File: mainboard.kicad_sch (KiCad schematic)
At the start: 94 parts, among them J1 Conn 02x05 1.27mm, J2 TMS-110-01-G-S, J3 SFMC-110-01-L-D, J4 CLP-105-02-X-DH-A, J5 CLP-105-02-X-DH-A, J6 CLP-105-02-X-DH-A, J7 CLP-105-02-X-DH-A, J8 U.FL-R-SMT-1, J9 USB_C_Receptacle_USB2.0, SW1 KMR231NG, SW2 SW_SPDT, U1 ATSAMD51J20A-M, U10 USBLC6-2SC6, U11 PCF8523TK, U2 MAX706RESA+, U3 AP2112K-3.3, U4 MR25H40, U5 BMX160, U6 RFM98PW, U7 DRV8830DRC, U8 DRV8830DRC, U9 DRV8830DRC, Y1 32.768kHz, Y2 32.768kHz

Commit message: Changes stash
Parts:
- removed D1: WS2812B, LED_SMD:LED_WS2812B_PLCC4_5.0x5.0mm_P3.2mm, symbol LED:WS2812B
- added C35: 1uF, Capacitor_SMD:C_0603_1608Metric, symbol Device:C_Small
- added D1: SK6812MINI, mainboard:NeoPixel 3535, symbol LED:SK6812MINI
- added J10: Micro_SD_Card, mainboard:MOLEX_503398-1892, symbol Connector:Micro_SD_Card
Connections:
- net +3V3: now also C35.2, D1.4 (VDD), J10.4 (VDD)
- net GND: now also C35.1, D1.2 (VSS), J10.6 (VSS), J10.9 (SHIELD)
- net SCL2: no longer U11.6 (SCL)
- net SDA2: no longer U11.5 (SDA)
- net SD_CS: now also J10.2 (DAT3/CD)
- net VUSB: no longer J2.8 (Pin_8), J3.16 (Pin_16), J4.10 (Pin_10), J5.10 (Pin_10), J6.10 (Pin_10), J7.10 (Pin_10)
- net at U1.42 (PA21): now also D1.3 (DIN)
- new net SCL_RTC: U11.6 (SCL)
- new net SDA_RTC: U11.5 (SDA)
- new net SD_MISO: J10.7 (DAT0)
- new net SD_MOSI: J10.3 (CMD)
- new net SD_SCK: J10.5 (CLK)
- no-connect marks 36 -> 44
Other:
- note added: "SD Card"

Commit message: Lots of updates
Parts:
- J10: footprint mainboard:MOLEX_503398-1892 -> mainboard:microSD_HC_Molex_104031-0811; symbol Connector:Micro_SD_Card -> Connector:Micro_SD_Card_Det
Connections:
- net F_MISO is gone; now on net FLASH_MISO: U4.2 (SO)
- net F_MOSI is gone; now on net FLASH_MOSI: U4.5 (SI)
- net F_SCK is gone; now on net FLASH_SCK: U4.6 (SCK)
- net CAM_CS: now also U1.11 (PB08); no longer J3.9 (Pin_9), U1.28 (PB15)
- net CAM_EN: no longer J3.15 (Pin_15)
- net GND: now also J10.10 (DET_A), J10.11 (SHIELD)
- net MISO: no longer J3.7 (Pin_7)
- net MOSI: no longer J3.5 (Pin_5)
- net SCK: no longer J3.3 (Pin_3)
- net SD_CS: now also U1.28 (PB15); no longer J3.11 (Pin_11), U1.11 (PB08)
- net at U2.1 (~{MR}): now also U2.8 (~{WDO})
- net at R12.2, U2.7 (~{RESET}): no longer U2.8 (~{WDO})
- net UART_TX: now reaches U1.63 (PB02)
- net UART_TX: now also J3.3 (Pin_3)
- net UART_RX: now reaches U1.64 (PB03)
- net UART_RX: now also J3.5 (Pin_5)
- net F_CS renamed FLASH_CS
- no-connect marks 44 -> 41
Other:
- note removed: "0xC0h(w) 0xC1h(r)"
- note removed: "0xC4h(w) 0xC5h(r)"
- note removed: "0xD0h(w) 0xD1h(r)"
- moved on the sheet: C12

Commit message: More updates
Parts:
- R1: value 10K -> 100K
- R12: value 10K -> 3.3K
- R2: value 330 -> 0
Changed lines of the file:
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@@
     (effects (font (size 1.27 1.27)) (justify right bottom))
   )
-  (text "WDT enabled\nwhen installed" (at 14.478 188.214 0)
+  (text "WDT enabled\nwhen installed" (at 13.716 188.214 0)
     (effects (font (size 0.889 0.889)) (justify left bottom))
   )
@@
     (in_bom yes) (on_board yes)
     (property "Reference" "R1" (id 0) (at 76.327 124.333 0))
-    (property "Value" "10K" (id 1) (at 76.835 126.365 0))
+    (property "Value" "100K" (id 1) (at 77.47 126.365 0))
     (property "Footprint" "Resistor_SMD:R_0603_1608Metric" (id 2) (at 72.39 125.095 90)
       (effects (font (size 1.27 1.27)) hide)
@@
     (in_bom yes) (on_board yes)
     (property "Reference" "R12" (id 0) (at 26.67 185.801 0))
-    (property "Value" "10K" (id 1) (at 26.67 187.833 0))
+    (property "Value" "3.3K" (id 1) (at 26.289 187.833 0))
     (property "Footprint" "Resistor_SMD:R_0603_1608Metric" (id 2) (at 29.21 186.563 90)
       (effects (font (size 1.27 1.27)) hide)
@@
     (in_bom yes) (on_board yes)
     (property "Reference" "R2" (id 0) (at 61.976 131.572 90))
-    (property "Value" "330" (id 1) (at 61.976 133.477 90))
+    (property "Value" "0" (id 1) (at 61.976 133.477 90))
     (property "Footprint" "Resistor_SMD:R_0603_1608Metric" (id 2) (at 61.722 130.175 90)
       (effects (font (size 1.27 1.27)) hide)
@@
     )
     (path "/00000000-0000-0000-0000-00005c6e5301"
-      (reference "R1") (unit 1) (value "10K") (footprint "Resistor_SMD:R_0603_1608Metric")
+      (reference "R1") (unit 1) (value "100K") (footprint "Resistor_SMD:R_0603_1608Metric")
     )
     (path "/1cbf010b-d192-4929-86a8-68a62710eb76"
-      (reference "R2") (unit 1) (value "330") (footprint "Resistor_SMD:R_0603_1608Metric")
+      (reference "R2") (unit 1) (value "0") (footprint "Resistor_SMD:R_0603_1608Metric")
     )
     (path "/00000000-0000-0000-0000-00005dc61a47"
@@
     )
     (path "/00000000-0000-0000-0000-00005dab9e18"
-      (reference "R12") (unit 1) (value "10K") (footprint "Resistor_SMD:R_0603_1608Metric")
+      (reference "R12") (unit 1) (value "3.3K") (footprint "Resistor_SMD:R_0603_1608Metric")
     )
     (path "/00000000-0000-0000-0000-00005f53229d"

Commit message: Finished routing
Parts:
- removed R2: 0, Resistor_SMD:R_0603_1608Metric, symbol Device:R_US
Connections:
- net CAM_EN is gone; now on net PAYLOAD_EN: U1.39 (PB16)
- net ~{RESET}: now also SW1.A (P), SW1.A' (P1)
- net PAYLOAD_EN: now reaches J3.7 (Pin_7)
- no-connect marks 41 -> 44
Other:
- note added: "Decoupling capacitors"
- note removed: "Decoupling capacitors (0603)"
- moved on the sheet: C1, C10, C11, C16, C18, C19, C2, C3, C34, C35, C4, C5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

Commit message: Some fixes
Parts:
- J3: footprint Connector_PinSocket_1.27mm:PinSocket_2x10_P1.27mm_Vertical -> mainboard:SAMTEC_SFC-110-T2-F-D-A-TR
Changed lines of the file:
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@@
     (property "Reference" "J3" (id 0) (at 345.948 103.632 0))
     (property "Value" "SFMC-110-01-L-D" (id 1) (at 346.075 132.842 0))
-    (property "Footprint" "Connector_PinSocket_1.27mm:PinSocket_2x10_P1.27mm_Vertical" (id 2) (at 344.932 116.84 0)
+    (property "Footprint" "mainboard:SAMTEC_SFC-110-T2-F-D-A-TR" (id 2) (at 344.932 116.84 0)
       (effects (font (size 1.27 1.27)) hide)
     )
@@
     )
     (path "/bd92b9d3-e82b-4176-883d-9f7ee4202081"
-      (reference "J3") (unit 1) (value "SFMC-110-01-L-D") (footprint "Connector_PinSocket_1.27mm:PinSocket_2x10_P1.27mm_Vertical")
+      (reference "J3") (unit 1) (value "SFMC-110-01-L-D") (footprint "mainboard:SAMTEC_SFC-110-T2-F-D-A-TR")
     )
     (path "/33ab456b-cf94-4695-907a-166a9700ece1"
@@
       (reference "Q18") (unit 1) (value "MMBT2907") (footprint "Package_TO_SOT_SMD:SOT-23")
     )
+    (path "/89e9ad27-deb2-49f4-bcf8-1a7a63ce9e3a/2fc32ae5-0f59-4b51-8220-4ec0d11d3fb5"
+      (reference "Q19") (unit 1) (value "BSS138DWQ-7") (footprint "Package_TO_SOT_SMD:SOT-363_SC-70-6")
+    )
+    (path "/89e9ad27-deb2-49f4-bcf8-1a7a63ce9e3a/013e9311-b29b-4c23-9447-12a0dfc99e64"
+      (reference "Q19") (unit 2) (value "BSS138DWQ-7") (footprint "Package_TO_SOT_SMD:SOT-363_SC-70-6")
+    )
     (path "/89e9ad27-deb2-49f4-bcf8-1a7a63ce9e3a/40202688-3447-41dd-b28a-6ee7d4dca54f"
       (reference "Q20") (unit 1) (value "BSS138DWQ-7") (footprint "Package_TO_SOT_SMD:SOT-363_SC-70-6")
@@
       (reference "Q21") (unit 2) (value "MBT2222ADW1T1") (footprint "Package_TO_SOT_SMD:SOT-363_SC-70-6")
     )
-    (path "/89e9ad27-deb2-49f4-bcf8-1a7a63ce9e3a/2fc32ae5-0f59-4b51-8220-4ec0d11d3fb5"
-      (reference "Q22") (unit 1) (value "BSS138DWQ-7") (footprint "Package_TO_SOT_SMD:SOT-363_SC-70-6")
-    )
-    (path "/89e9ad27-deb2-49f4-bcf8-1a7a63ce9e3a/013e9311-b29b-4c23-9447-12a0dfc99e64"
-      (reference "Q22") (unit 2) (value "BSS138DWQ-7") (footprint "Package_TO_SOT_SMD:SOT-363_SC-70-6")
-    )
     (path "/89e9ad27-deb2-49f4-bcf8-1a7a63ce9e3a/7d0ba366-3197-4fe2-802c-584a9272a77a"
-      (reference "Q23") (unit 1) (value "MBT2222ADW1T1") (footprint "Package_TO_SOT_SMD:SOT-363_SC-70-6")
+      (reference "Q22") (unit 1) (value "MBT2222ADW1T1") (footprint "Package_TO_SOT_SMD:SOT-363_SC-70-6")
     )
     (path "/89e9ad27-deb2-49f4-bcf8-1a7a63ce9e3a/a5ae381c-2593-4678-8b67-af85f16c72b1"
-      (reference "Q23") (unit 2) (value "MBT2222ADW1T1") (footprint "Package_TO_SOT_SMD:SOT-363_SC-70-6")
+      (reference "Q22") (unit 2) (value "MBT2222ADW1T1") (footprint "Package_TO_SOT_SMD:SOT-363_SC-70-6")
     )
     (path "/00000000-0000-0000-0000-00005c6e5301"
       (reference "R1") (unit 1) (value "100K") (footprint "Resistor_SMD:R_0603_1608Metric")
     )
+    (path "/89e9ad27-deb2-49f4-bcf8-1a7a63ce9e3a/f4a81e09-a91f-4348-bdf4-5c5addec82b1"
+      (reference "R2") (unit 1) (value "200K") (footprint "Resistor_SMD:R_0603_1608Metric")
+    )
     (path "/00000000-0000-0000-0000-00005dc61a47"
       (reference "R3") (unit 1) (value "100K") (footprint "Resistor_SMD:R_0603_1608Metric")
@@
       (reference "R106") (unit 1) (value "10K") (footprint "Resistor_SMD:R_0603_1608Metric")
     )
-    (path "/89e9ad27-deb2-49f4-bcf8-1a7a63ce9e3a/f4a81e09-a91f-4348-bdf4-5c5addec82b1"
-      (reference "R107") (unit 1) (value "200K") (footprint "Resistor_SMD:R_0603_1608Metric")
-    )
     (path "/00000000-0000-0000-0000-00005c6b86a4"

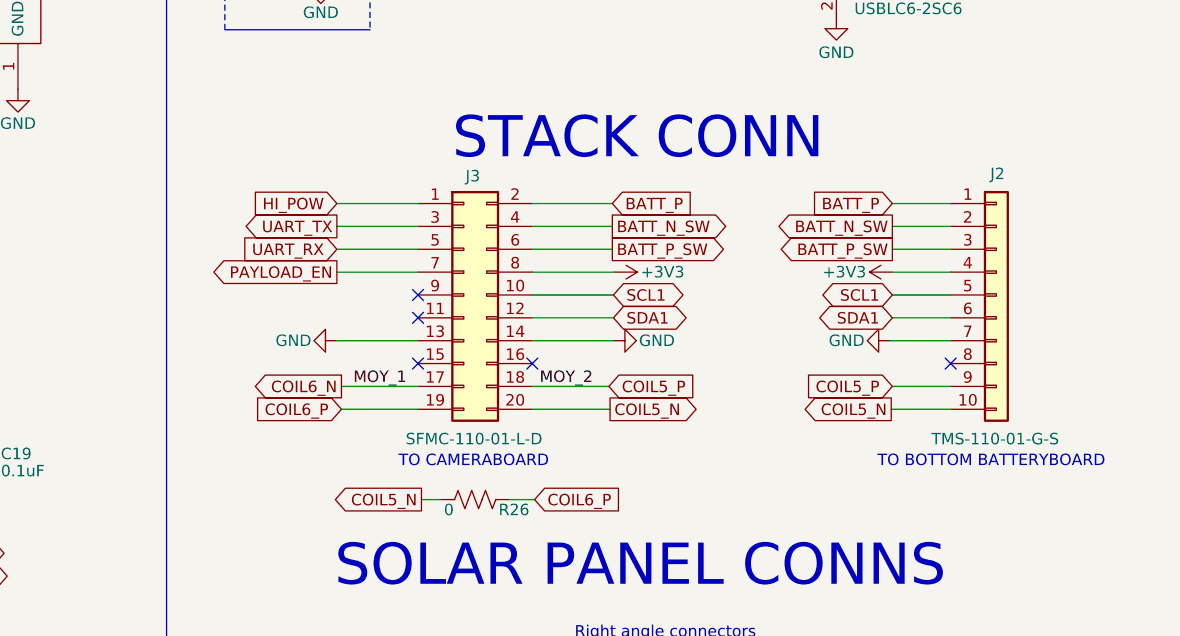
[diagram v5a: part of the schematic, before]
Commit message: Changed stack connectors to SMD ones
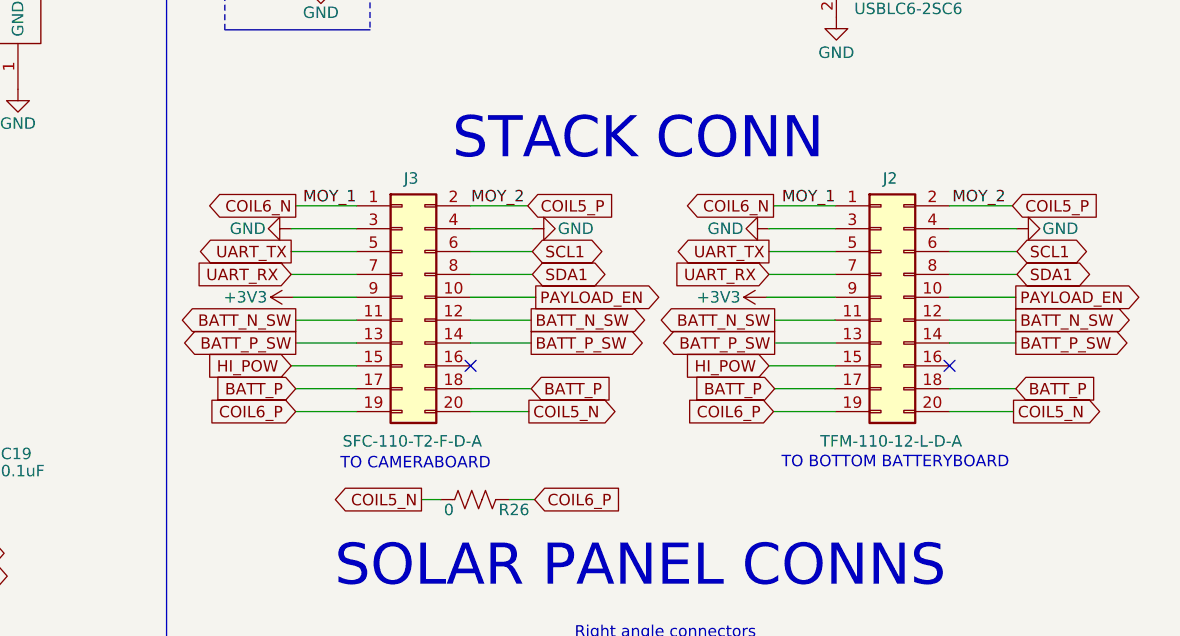
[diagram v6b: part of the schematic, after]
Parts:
- removed J2: TMS-110-01-G-S, Connector_PinSocket_1.27mm:PinSocket_1x10_P1.27mm_Vertical, symbol Connector_Generic:Conn_01x10
- added J2: TFM-110-12-L-D-A, mainboard:SAMTEC_TFM-110-12-L-D-A, symbol Connector_Generic:Conn_02x10_Odd_Even
- J3: value SFMC-110-01-L-D -> SFC-110-T2-F-D-A
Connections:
- net +3V3: now also J3.9 (Pin_9), J2.9 (Pin_9); no longer J3.8 (Pin_8)
- net BATT_N_SW: now also J3.11 (Pin_11), J3.12 (Pin_12), J2.11 (Pin_11), J2.12 (Pin_12); no longer J3.4 (Pin_4)
- net BATT_P: now also J3.17 (Pin_17), J3.18 (Pin_18), J2.17 (Pin_17), J2.18 (Pin_18); no longer J3.2 (Pin_2)
- net BATT_P_SW: now also J3.13 (Pin_13), J3.14 (Pin_14), J2.13 (Pin_13), J2.14 (Pin_14); no longer J3.6 (Pin_6)
- net COIL5_N: now also J2.20 (Pin_20)
- net COIL5_P: now also J3.2 (Pin_2), J2.2 (Pin_2); no longer J3.18 (Pin_18)
- net COIL6_N: now also J3.1 (Pin_1), J2.1 (Pin_1); no longer J3.17 (Pin_17)
- net COIL6_P: now also J2.19 (Pin_19)
- net GND: now also J3.3 (Pin_3), J3.4 (Pin_4), J2.3 (Pin_3), J2.4 (Pin_4); no longer J3.13 (Pin_13), J3.14 (Pin_14)
- net HI_POW: now also J3.15 (Pin_15), J2.15 (Pin_15); no longer J3.1 (Pin_1)
- net PAYLOAD_EN: now also J3.10 (Pin_10), J2.10 (Pin_10); no longer J3.7 (Pin_7)
- net SCL1: now also J3.6 (Pin_6), J2.6 (Pin_6); no longer J3.10 (Pin_10)
- net SDA1: now also J3.8 (Pin_8), J2.8 (Pin_8); no longer J3.12 (Pin_12)
- net UART_RX: now also J3.7 (Pin_7), J2.7 (Pin_7); no longer J3.5 (Pin_5)
- net UART_TX: now also J3.5 (Pin_5), J2.5 (Pin_5); no longer J3.3 (Pin_3)
- no-connect marks 44 -> 41
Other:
- moved on the sheet: J3

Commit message: Finished B2/01 Updates
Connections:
- net +3V3: now also J2.10 (Pin_10), J3.10 (Pin_10), R16.1
- net BATT_P: now also J4.10 (Pin_10), J5.10 (Pin_10), J6.10 (Pin_10), J7.10 (Pin_10)
- net BURN2: no longer J4.4 (Pin_4), J5.4 (Pin_4), J6.4 (Pin_4), J7.4 (Pin_4)
- net GND: now also J2.16 (Pin_16), J3.16 (Pin_16), J4.4 (Pin_4), J5.4 (Pin_4), J6.4 (Pin_4), J7.4 (Pin_4); no longer R16.1
- net HI_POW: no longer J2.15 (Pin_15), J3.15 (Pin_15)
- net PAYLOAD_EN: now also J2.15 (Pin_15), J3.15 (Pin_15); no longer J2.10 (Pin_10), J3.10 (Pin_10)
- no-connect marks 41 -> 35
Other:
- note added: "0x69"
- note added: "TO PAYLOADBOARD"
- note removed: "TO CAMERABOARD"
- moved on the sheet: C18
